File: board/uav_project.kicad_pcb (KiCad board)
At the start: 2 copper layers, 0 parts

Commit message: Started work on PCB design, more work on rewritting firmware to be semi usable
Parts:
- added C10: 1p, Capacitor_SMD:C_0603_1608Metric, F.Cu at (123.7, 142.4)
- added C11: 100n, Capacitor_SMD:C_0603_1608Metric, F.Cu at (123.7, 144.9)
- added C12: 100p, Capacitor_SMD:C_0603_1608Metric, F.Cu at (123.7, 147.4)
- added C14: 100n, Capacitor_SMD:C_0603_1608Metric, F.Cu at (171.4, 59.6)
- added C15: 100u, Capacitor_SMD:C_0603_1608Metric, F.Cu at (56.8, 79.0)
- added C16: 1p, Capacitor_SMD:C_0603_1608Metric, F.Cu at (123.7, 149.9)
- added C2: 100n, Capacitor_SMD:C_0603_1608Metric, F.Cu at (56.8, 71.5)
- added C3: 100n, Capacitor_SMD:C_0603_1608Metric, F.Cu at (56.8, 74.0)
- added C4: 100u, Capacitor_THT:CP_Radial_D8.0mm_P3.50mm, F.Cu at (100.2, 90.8)
- added C5: 100n, Capacitor_SMD:C_0201_0603Metric, F.Cu at (143.0, 29.2)
- added C6: 33u, Capacitor_THT:CP_Radial_D5.0mm_P2.50mm, F.Cu at (169.3, 153.2)
- added C7: 100n, Capacitor_SMD:C_0603_1608Metric, F.Cu at (123.7, 137.4)
- added C8: 100n, Capacitor_SMD:C_0603_1608Metric, F.Cu at (56.8, 76.5)
- added C9: 100n, Capacitor_SMD:C_0603_1608Metric, F.Cu at (123.7, 139.9)
- added D1: 1N53xxB, Diode_THT:D_DO-201_P3.81mm_Vertical_AnodeUp, F.Cu at (141.7, 114.3)
- added D3: LED, LED_SMD:LED_0805_2012Metric, F.Cu at (137.3, 29.9)
- added D4: LED, LED_SMD:LED_0805_2012Metric, F.Cu at (118.3, 155.2)
- added D6: SS210, Diode_SMD:D_SMB, F.Cu at (142.2, 48.3)
- added F1: Fuse, Fuse:Fuseholder_Clip-5x20mm_Littelfuse_111_Lateral_P18.80x5.00mm_D1.17mm_Horizontal, B.Cu at (104.6, 122.4)
- added F2: Polyfuse, Fuse:Fuse_1210_3225Metric, F.Cu at (61.6, 78.9)
- added H1: MountingHole, MountingHole:MountingHole_2.2mm_M2, F.Cu at (187.5, 67.5)
- added H2: MountingHole, MountingHole:MountingHole_2.2mm_M2, F.Cu at (187.5, 122.5)
- added H3: MountingHole, MountingHole:MountingHole_2.2mm_M2, F.Cu at (92.5, 67.5)
- added H4: MountingHole, MountingHole:MountingHole_2.2mm_M2, F.Cu at (92.5, 122.5)
- added IC1: RT9193-33GB, Package_TO_SOT_SMD:SOT-23-5, F.Cu at (108.9, 155.9)
- added IC2: NJG1130KA1-TE1, Imported_Footprints:SOTFL50P160X60-6N, F.Cu at (113.2, 157.9)
- added J2: Conn_01x08_Pin, Connector_PinHeader_1.00mm:PinHeader_1x08_P1.00mm_Vertical, F.Cu at (167.8, 59.8)
- added J3: Bat IN Terminal, TerminalBlock:TerminalBlock_bornier-2_P5.08mm, F.Cu at (95.0, 108.7)
- added J4: Bat OUT Terminal, TerminalBlock:TerminalBlock_bornier-2_P5.08mm, F.Cu at (95.0, 97.0)
- added J5: Conn_Coaxial, Connector_Coaxial:U.FL_Molex_MCRF_73412-0110_Vertical, F.Cu at (124.7, 154.2)
- added JP1: SolderJumper_2_Open, Jumper:SolderJumper-2_P1.3mm_Open_Pad1.0x1.5mm, F.Cu at (165.0, 140.5)
- added JP2: SolderJumper_2_Open, Jumper:SolderJumper-2_P1.3mm_Open_Pad1.0x1.5mm, F.Cu at (165.0, 144.1)
- added JP3: SolderJumper_2_Open, Jumper:SolderJumper-2_P1.3mm_Open_Pad1.0x1.5mm, F.Cu at (165.0, 147.6)
- added JP4: SolderJumper_2_Open, Jumper:SolderJumper-2_P1.3mm_Open_Pad1.0x1.5mm, F.Cu at (165.0, 151.2)
- added L1: 47u, Inductor_SMD:L_7.3x7.3_H3.5, F.Cu at (91.5, 57.6)
- added L2: 8.7n, Inductor_SMD:L_0603_1608Metric, F.Cu at (127.7, 137.4)
- added L3: 8.7n, Inductor_SMD:L_0603_1608Metric, F.Cu at (127.7, 139.9)
- added L4: 18n, Inductor_SMD:L_0805_2012Metric, F.Cu at (113.8, 155.1)
- added L5: 47n, Inductor_SMD:L_0603_1608Metric, F.Cu at (127.7, 142.4)
- added Q1: PMOS, Package_TO_SOT_THT:TO-220-3_Vertical, F.Cu at (130.6, 116.3)
- added R1: 20m, Resistor_SMD:R_1210_3225Metric, F.Cu at (98.3, 40.0)
- added R10: 220, Resistor_SMD:R_0603_1608Metric, F.Cu at (152.8, 150.0)
- added R11: 220, Resistor_SMD:R_0603_1608Metric, F.Cu at (152.8, 152.5)
- added R12: 220, Resistor_SMD:R_0603_1608Metric, F.Cu at (156.8, 140.0)
- added R13: 220, Resistor_SMD:R_0603_1608Metric, F.Cu at (156.8, 142.5)
- added R14: 220, Resistor_SMD:R_0603_1608Metric, F.Cu at (156.8, 145.0)
- added R15: 220, Resistor_SMD:R_0603_1608Metric, F.Cu at (156.8, 147.5)
- added R16: 220, Resistor_SMD:R_0603_1608Metric, F.Cu at (156.8, 150.0)
- added R17: 220, Resistor_SMD:R_0603_1608Metric, F.Cu at (156.8, 152.5)
- added R18: 220, Resistor_SMD:R_0603_1608Metric, F.Cu at (160.8, 140.0)
- added R19: 220, Resistor_SMD:R_0603_1608Metric, F.Cu at (160.8, 142.5)
- added R2: 20m, Resistor_SMD:R_1210_3225Metric, F.Cu at (103.9, 107.8)
- added R20: 220, Resistor_SMD:R_0603_1608Metric, F.Cu at (160.8, 145.0)
- added R21: 220, Resistor_SMD:R_0603_1608Metric, F.Cu at (160.8, 147.5)
- added R22: 220, Resistor_SMD:R_0603_1608Metric, F.Cu at (160.8, 150.0)
- added R23: 10, Resistor_SMD:R_0603_1608Metric, F.Cu at (127.7, 144.9)
- added R24: 4.7k, Resistor_SMD:R_0603_1608Metric, F.Cu at (171.4, 62.1)
- added R25: 4.7k, Resistor_SMD:R_0603_1608Metric, F.Cu at (171.4, 64.6)
- added R26: 470, Resistor_SMD:R_0603_1608Metric, F.Cu at (127.7, 147.4)
- added R3: 100, Resistor_SMD:R_1206_3216Metric, F.Cu at (138.7, 121.9)
- added R4: 10k, Resistor_SMD:R_1206_3216Metric, F.Cu at (103.5, 40.2)
- added R4: 10k, Resistor_SMD:R_1206_3216Metric, F.Cu at (143.8, 121.9)
- added R5: 10k, Resistor_SMD:R_0603_1608Metric, F.Cu at (152.8, 140.0)
- added R6: 470, Resistor_SMD:R_0603_1608Metric, F.Cu at (56.8, 81.5)
- added R7: 220, Resistor_SMD:R_0603_1608Metric, F.Cu at (152.8, 142.5)
- added R8: 220, Resistor_SMD:R_0603_1608Metric, F.Cu at (152.8, 145.0)
- added R9: 220, Resistor_SMD:R_0603_1608Metric, F.Cu at (152.8, 147.5)
- added TVS1: SMAJ30CA, Diode_SMD:D_SMA, F.Cu at (132.1, 121.9)
- added TVS10: SMAJ30CA, Diode_SMD:D_SMA, F.Cu at (38.0, 78.2)
- added TVS3: SMAJ30CA, Diode_SMD:D_SMA, F.Cu at (38.0, 46.4)
- added TVS4: SMAJ30CA, Diode_SMD:D_SMA, F.Cu at (38.0, 50.9)
- added TVS5: SMAJ30CA, Diode_SMD:D_SMA, F.Cu at (38.0, 55.5)
- added TVS6: SMAJ30CA, Diode_SMD:D_SMA, F.Cu at (38.0, 60.0)
- added TVS7: SMAJ30CA, Diode_SMD:D_SMA, F.Cu at (38.0, 64.5)
- added TVS8: SMAJ30CA, Diode_SMD:D_SMA, F.Cu at (38.0, 69.1)
- added TVS9: SMAJ30CA, Diode_SMD:D_SMA, F.Cu at (38.0, 73.7)
- added U1: INA226, Package_SO:VSSOP-10_3x3mm_P0.5mm, F.Cu at (125.2, 58.7)
- added U2: AMS1117-3.3, Package_TO_SOT_SMD:SOT-223-3_TabPin2, F.Cu at (81.8, 57.4)
- added U3: INA226, Package_SO:VSSOP-10_3x3mm_P0.5mm, F.Cu at (110.2, 107.7)
- added U4: LM2596S-5, Package_TO_SOT_SMD:TO-263-5_TabPin3, F.Cu at (105.7, 81.0)
- added U5: PCA9685PW, Package_SO:TSSOP-28_4.4x9.7mm_P0.65mm, F.Cu at (117.5, 75.6)
- added U6: NEO-M7N, RF_GPS:ublox_NEO, F.Cu at (156.8, 75.8)
- added WT901B1: ~, Custom_Footprints:WT901B, F.Cu at (149.9, 95.0)
- added conn_3x1: conn_03x04_Pin, Custom_Footprints:PinHeader_3x04, F.Cu at (153.7, 133.6)
- added conn_3x2: conn_03x04_Pin, Custom_Footprints:PinHeader_3x04, F.Cu at (159.0, 133.6)
- added conn_3x3: conn_03x04_Pin, Custom_Footprints:PinHeader_3x04, F.Cu at (164.3, 133.6)
- added conn_3x4: conn_03x04_Pin, Custom_Footprints:PinHeader_3x04, F.Cu at (169.6, 133.6)
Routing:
- net Net-(D1-A): track 0.00 -> 13.6 mm
- net /Power managment/BAT SENSE OUT: track 0.00 -> 9.67 mm
- net Net-(Q1-G): track 0.00 -> 7.37 mm
- net /Power managment/BAT SENSE IN: track 0.00 -> 4.49 mm
- net GND: track 0.00 -> 3.07 mm, vias 0 -> 2
- net (no net): track 0.00 -> 0.72 mm
- added copper zone on F.Cu, net /Power managment/BAT SENSE IN
- added copper zone on F.Cu, net /Power managment/BAT SENSE OUT
- added copper zone on F.Cu, net /Power managment/BAT UNSAFE
- added copper zone on B.Cu, net GND
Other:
- board outline added: 100 x 60 mm

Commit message: More work on PCB design
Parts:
- removed C5: 100n, Capacitor_SMD:C_0201_0603Metric
- removed J2: Conn_01x08_Pin, Connector_PinHeader_1.00mm:PinHeader_1x08_P1.00mm_Vertical
- removed JP1, JP2, JP3, JP4: SolderJumper_2_Open, Jumper:SolderJumper-2_P1.3mm_Open_Pad1.0x1.5mm
- removed TVS4: SMAJ30CA, Diode_SMD:D_SMA
- added C1: 100n, Capacitor_SMD:C_0603_1608Metric, F.Cu at (100.4, 83.5)
- added J1: Conn_01x07, Connector_PinHeader_1.00mm:PinHeader_1x07_P1.00mm_Vertical, F.Cu at (163.9, 114.3)
- C15: footprint Capacitor_SMD:C_0603_1608Metric -> Capacitor_THT:CP_Radial_D8.0mm_P3.50mm
- moved TVS3 157.9 mm to (177.0, 121.2), turned to -90 degrees
- moved TVS5 150.1 mm to (172.9, 121.2), turned to -90 degrees
- moved TVS6 144.0 mm to (168.3, 121.2), turned to -90 degrees
- moved TVS7 138.0 mm to (163.8, 121.2), turned to -90 degrees
- moved TVS8 132.0 mm to (159.2, 121.2), turned to -90 degrees
- moved TVS9 126.0 mm to (154.7, 121.2), turned to -90 degrees
- moved IC2 124.1 mm to (195.3, 64.8)
- moved TVS10 120.1 mm to (150.2, 121.2), turned to -90 degrees
- moved L2 119.5 mm to (195.6, 39.1)
- moved L5 119.5 mm to (195.6, 44.1)
- moved R23 119.5 mm to (195.6, 46.6)
- moved C10 119.5 mm to (191.6, 44.1)
- moved C11 119.5 mm to (191.6, 46.6)
- moved C16 119.5 mm to (191.6, 51.6)
- moved C7 119.5 mm to (191.6, 39.1)
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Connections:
- TVS10 pad 1: TX -> GND
- TVS3 pad 1: +3V3 -> SLC
- TVS5 pad 1: +5V -> SDA
- TVS6 pad 1: GND -> RX
- TVS7 pad 1: SLC -> TX
- TVS8 pad 1: SDA -> +3V3
- TVS9 pad 1: RX -> +5V
- conn_3x4 pad 11: Net-(JP4-A) -> +5V
- conn_3x4 pad 2: Net-(JP1-A) -> +5V
- conn_3x4 pad 5: Net-(JP2-A) -> +5V
- conn_3x4 pad 8: Net-(JP3-A) -> +5V
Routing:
- net +5V: track 0.00 -> 102.8 mm
- net GND: track 3.07 -> 49.3 mm, vias 2 -> 37
- net Net-(U4-FB): track 0.00 -> 36.0 mm
- net +3V3: track 0.00 -> 25.1 mm, vias 0 -> 3
- net Net-(D6-K): track 0.00 -> 21.6 mm
- net /Power managment/5V SENSE IN: track 0.00 -> 16.8 mm
- net SLC: track 0.00 -> 16.3 mm
- net SDA: track 0.00 -> 15.2 mm
- net /Power managment/BAT SENSE OUT: track 9.67 -> 22.7 mm
- net TX: track 0.00 -> 6.18 mm
- net RX: track 0.00 -> 5.09 mm
- net Net-(R10-Pad1): track 0.00 -> 3.30 mm
- net Net-(R9-Pad1): track 0.00 -> 2.68 mm
- net Net-(R8-Pad1): track 0.00 -> 2.34 mm
- net Net-(U5-~{OE}): track 0.00 -> 2.19 mm
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
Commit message: First version of PCB finished
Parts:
- removed C9: 100n, Capacitor_SMD:C_0603_1608Metric
- removed the R4 at (143.8, 121.9)
- R2: footprint Resistor_SMD:R_1210_3225Metric -> Resistor_SMD:R_2512_6332Metric
- moved R4 110.5 mm to (143.9, 121.9)
- moved C3 72.9 mm to (127.0, 93.6), turned to 180 degrees
- moved C7 69.0 mm to (137.2, 81.5)
- moved R6 64.0 mm to (118.8, 97.4), turned to 90 degrees
- moved C16 63.9 mm to (133.9, 79.0), turned to -90 degrees
- moved D3 62.3 mm to (118.9, 93.9), turned to -90 degrees
- moved C10 62.1 mm to (137.7, 74.9)
- moved R25 61.3 mm to (124.5, 103.9), turned to -90 degrees
- moved R24 61.0 mm to (127.0, 103.9), turned to -90 degrees
- moved L3 55.5 mm to (158.8, 83.1), turned to -90 degrees
- moved C14 54.7 mm to (132.1, 97.5), turned to -90 degrees
- moved L2 52.3 mm to (158.8, 76.2), turned to -90 degrees
- moved R26 49.0 mm to (156.0, 77.9), turned to 90 degrees
- moved L5 46.8 mm to (158.7, 72.9), turned to 90 degrees
- moved C11 46.5 mm to (158.7, 79.5), turned to -90 degrees
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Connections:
- C16 pad 2: +3.3V -> +3V3
- D4 pad 2: /GPS module/+3V3 LN -> Net-(D4-A)
- IC1 pad 1: +3.3V -> +3V3
- IC1 pad 3: +3.3V -> +3V3
- IC2 pad 2: unconnected-(IC2-GND_1-Pad2) -> GND
- J1 pad 4: TX -> SDA
- J1 pad 5: RX -> SLC
- J1 pad 6: SDA -> TX
- J1 pad 7: SLC -> RX
- R11 pad 2: /Servo driver/PWM4 -> /Servo driver/PWM7
- R12 pad 2: /Servo driver/PWM5 -> /Servo driver/PWM6
- R13 pad 2: /Servo driver/PWM6 -> /Servo driver/PWM5
- R14 pad 2: /Servo driver/PWM7 -> /Servo driver/PWM4
- R26 pad 1: Net-(U6-TIMEPULSE) -> Net-(D4-A)
- R26 pad 2: Net-(D4-K) -> /GPS module/+3V3 LN
- TVS3 pad 1: SLC -> RX
- TVS5 pad 1: SDA -> TX
- TVS6 pad 1: RX -> SLC
- TVS7 pad 1: TX -> SDA
- U1 pad 2: +3V3 -> SDA
- U3 pad 2: +3V3 -> SLC
- U5 pad 2: GND -> +5V
- U5 pad 24: +5V -> GND
- U5 pad 4: +5V -> GND
- U6 pad 2: +3V3 -> /GPS module/+3V3 LN
- U6 pad 3: Net-(U6-TIMEPULSE) -> Net-(D4-K)
- conn_3x2 pad 1: Net-(R15-Pad1) -> Net-(R18-Pad1)
- conn_3x2 pad 10: Net-(R18-Pad1) -> Net-(R15-Pad1)
- conn_3x2 pad 4: Net-(R16-Pad1) -> Net-(R17-Pad1)
- conn_3x2 pad 7: Net-(R17-Pad1) -> Net-(R16-Pad1)
- conn_3x3 pad 1: Net-(R11-Pad1) -> Net-(R14-Pad1)
- conn_3x3 pad 10: Net-(R14-Pad1) -> Net-(R11-Pad1)
- conn_3x3 pad 4: Net-(R12-Pad1) -> Net-(R13-Pad1)
- conn_3x3 pad 7: Net-(R13-Pad1) -> Net-(R12-Pad1)
- conn_3x4 pad 1: Net-(R19-Pad1) -> Net-(R22-Pad1)
- conn_3x4 pad 10: Net-(R22-Pad1) -> Net-(R19-Pad1)
- conn_3x4 pad 4: Net-(R20-Pad1) -> Net-(R21-Pad1)
- conn_3x4 pad 7: Net-(R21-Pad1) -> Net-(R20-Pad1)
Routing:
- net SDA: track 15.2 -> 133.0 mm, vias 0 -> 6
- net +3V3: track 25.1 -> 125.8 mm, vias 3 -> 6
- net SLC: track 16.3 -> 109.6 mm, vias 0 -> 4
- net GND: track 49.3 -> 137.2 mm, vias 37 -> 81
- net /GPS module/+3V3 LN: track 0.00 -> 59.1 mm
- net +5V: track 102.8 -> 156.5 mm, vias 0 -> 2
- net RX: track 5.09 -> 43.1 mm
- net TX: track 6.18 -> 43.6 mm
- net /Servo driver/PWM0: track 0.00 -> 22.3 mm
- net /Servo driver/PWM1: track 0.00 -> 21.8 mm
- net /Servo driver/PWM2: track 0.00 -> 21.0 mm
- net /Servo driver/PWM7: track 0.00 -> 20.8 mm
- net /Servo driver/PWM15: track 0.00 -> 20.3 mm
- net /Servo driver/PWM3: track 0.00 -> 19.9 mm
- net /Servo driver/PWM6: track 0.00 -> 19.9 mm
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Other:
- board size 100 x 60 mm -> 80 x 59.9 mm

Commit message: Minor improvements to board design
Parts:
- removed TVS10: SMAJ30CA, Diode_SMD:D_SMA
- removed WT901B1: ~, Custom_Footprints:WT901B
- removed conn_3x1, conn_3x2, conn_3x3, conn_3x4: conn_03x04_Pin, Custom_Footprints:PinHeader_3x04
- added PWM1: conn_03x04_Pin, Custom_Footprints:PinHeader_3x04, F.Cu at (123.1, 67.4)
- added PWM2: conn_03x04_Pin, Custom_Footprints:PinHeader_3x04, F.Cu at (129.7, 67.3)
- added PWM3: conn_03x04_Pin, Custom_Footprints:PinHeader_3x04, F.Cu at (116.3, 67.3)
- added PWM4: conn_03x04_Pin, Custom_Footprints:PinHeader_3x04, F.Cu at (109.7, 67.3)
- added U7: WT901B, Custom_Footprints:WT901B, F.Cu at (129.4, 95.5)
- F1: moved to F.Cu
- R1: footprint Resistor_SMD:R_1210_3225Metric -> Resistor_SMD:R_1206_3216Metric
- moved F1 4.96 mm to (104.6, 117.4)
- moved R3 1.72 mm to (140.4, 121.9)
- moved R4 1.72 mm to (145.6, 121.9)
- moved C14 1.47 mm to (131.3, 98.8)
- moved C1 0.65 mm to (99.7, 83.5)
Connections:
- J1 pad 2: +5V -> +3V3
- J1 pad 3: +3V3 -> +5V
- TVS8 pad 1: +3V3 -> +5V
- TVS9 pad 1: +5V -> +3V3
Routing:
- net GND: track 137.2 -> 88.9 mm
- net +3V3: track 125.8 -> 145.9 mm, vias 6 -> 4
- net +5V: track 156.5 -> 164.8 mm
- net Net-(U4-FB): track 36.0 -> 44.3 mm
- net Net-(Q1-G): track 7.37 -> 10.9 mm
- net SLC: track 109.6 -> 112.2 mm
- net Net-(IC1-BP): track 2.20 -> 4.55 mm
- net Net-(D4-K): track 2.51 -> 4.28 mm
- net Net-(D1-A): track 13.6 -> 11.9 mm
- net RX: track 43.1 -> 44.6 mm
- net /GPS module/+3V3 LN: track 59.1 -> 60.0 mm
- net /Servo driver/PWM7: track 20.8 -> 21.5 mm
- net /Power managment/BAT SENSE OUT: track 32.0 -> 32.6 mm
- net Net-(PWM2-Pad7): track 3.48 -> 4.11 mm
- net Net-(U5-~{OE}): track 3.00 -> 3.59 mm
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
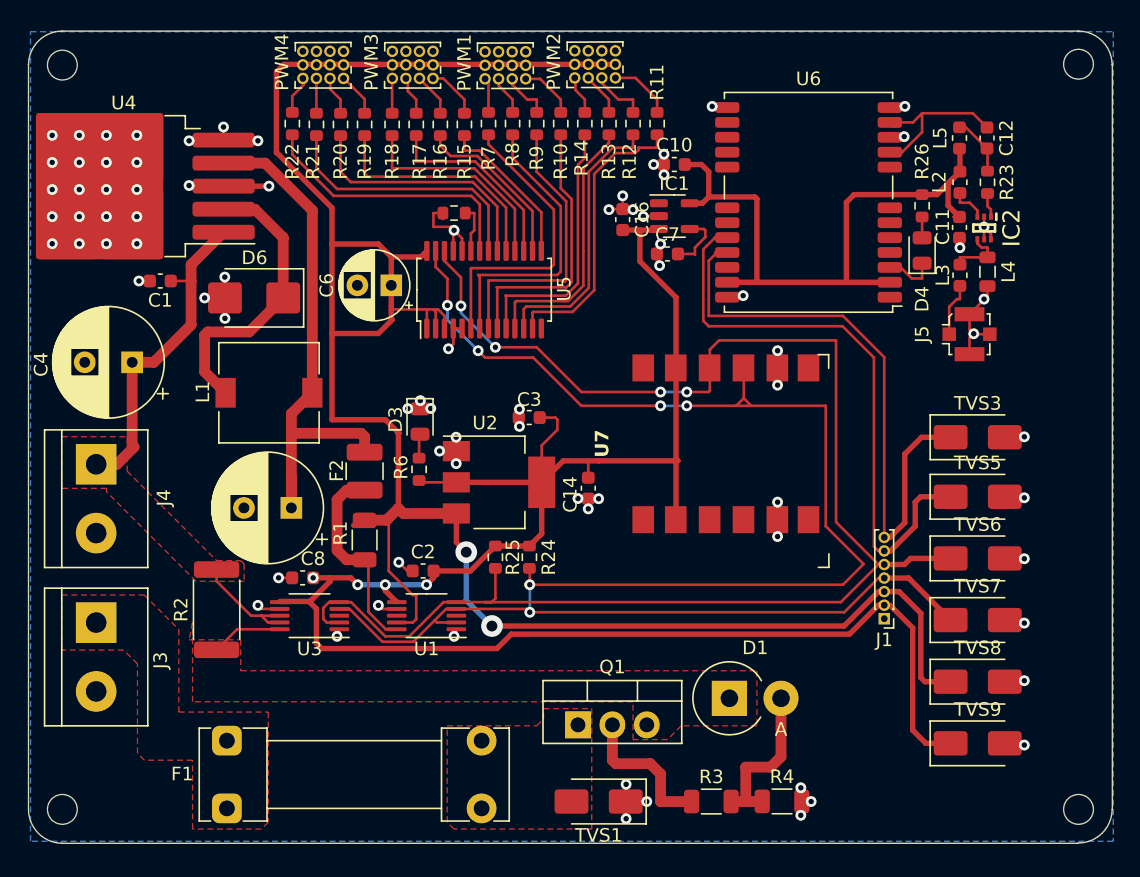
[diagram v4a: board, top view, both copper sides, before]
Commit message: Put some more space between 16V and 5V line
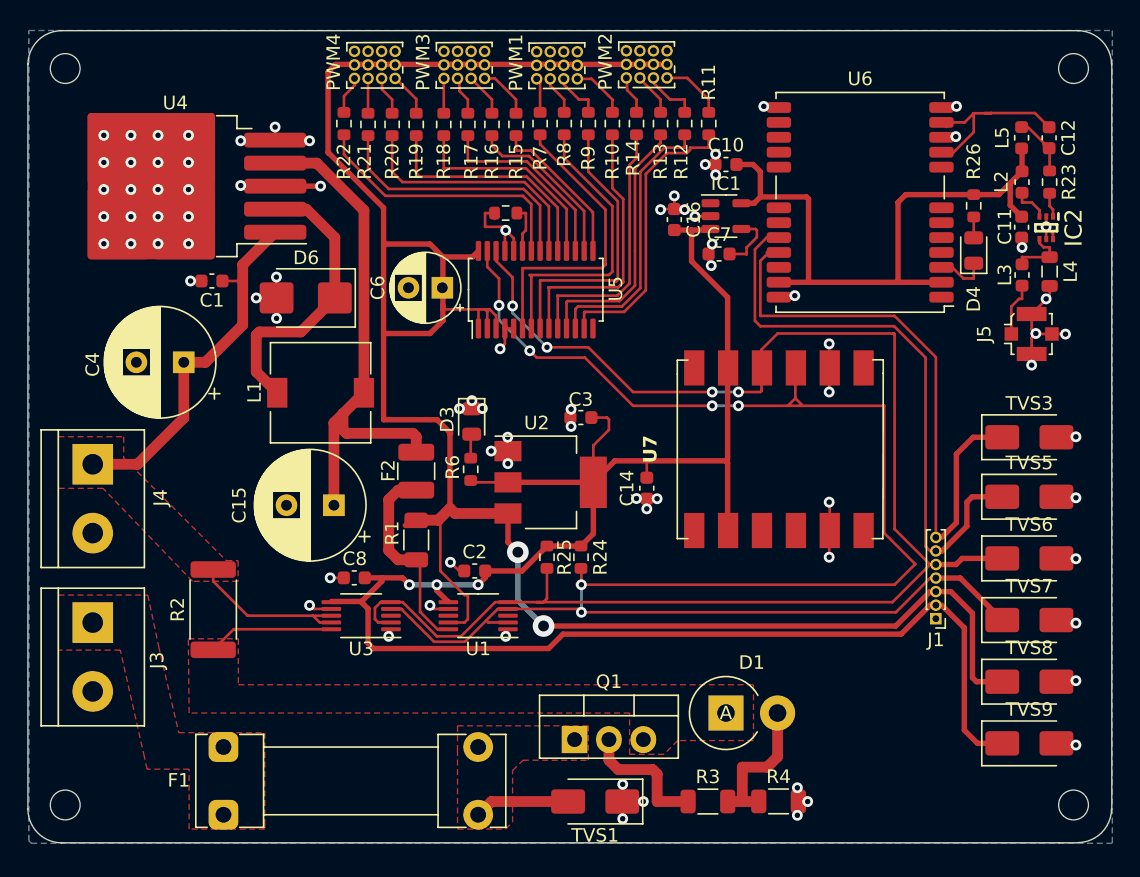
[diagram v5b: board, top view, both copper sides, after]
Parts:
- moved C11 4.58 mm to (163.3, 79.5)
- moved C12 4.58 mm to (165.3, 72.9)
- moved IC2 4.58 mm to (165.1, 79.6)
- moved J5 4.58 mm to (164.0, 87.4)
- moved L2 4.58 mm to (163.3, 76.2)
- moved L3 4.58 mm to (163.3, 83.1)
- moved L4 4.58 mm to (165.4, 82.8)
- moved L5 4.58 mm to (163.3, 72.9)
- moved R23 4.58 mm to (165.4, 76.2)
- moved C14 4.32 mm to (135.6, 98.8)
- moved U7 4.03 mm to (133.4, 95.9)
- moved C3 3.81 mm to (130.8, 93.6)
- moved R25 3.81 mm to (128.3, 103.9)
- moved R9 3.81 mm to (131.3, 71.9)
- moved C1 3.81 mm to (103.5, 83.5)
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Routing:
- net /Power managment/BAT UNSAFE: track 0.00 -> 7.04 mm
- net /Power managment/BAT SENSE OUT: track 32.6 -> 39.3 mm
- net Net-(U4-FB): track 44.3 -> 38.6 mm
- net GND: track 88.9 -> 93.3 mm, vias 81 -> 83
- net /Power managment/BAT SENSE IN: track 5.29 -> 9.35 mm
- net /GPS module/RF_IN: track 12.3 -> 13.6 mm
- net Net-(Q1-G): track 10.9 -> 9.82 mm
- net Net-(D1-A): track 11.9 -> 10.8 mm
- net SLC: track 112.2 -> 113.1 mm
- net +3V3: track 145.9 -> 145.5 mm, vias 4 -> 3
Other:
- outline, holes or cut-outs redrawn
